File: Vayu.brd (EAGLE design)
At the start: 27 x 80 mm, 63 parts, among them J1 1770911, J2 1770911, J3 3220-10-0100-00, J4 SM04B-SRSS-TB(LF)(SN), Q1 IRLML6402TRPBF, Q2 IRLML6402TRPBF, Q3 IRLML6402TRPBF, Q4 IRLML6402TRPBF, SW1 TL1105LF160Q, SW2 TL1105LF160Q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

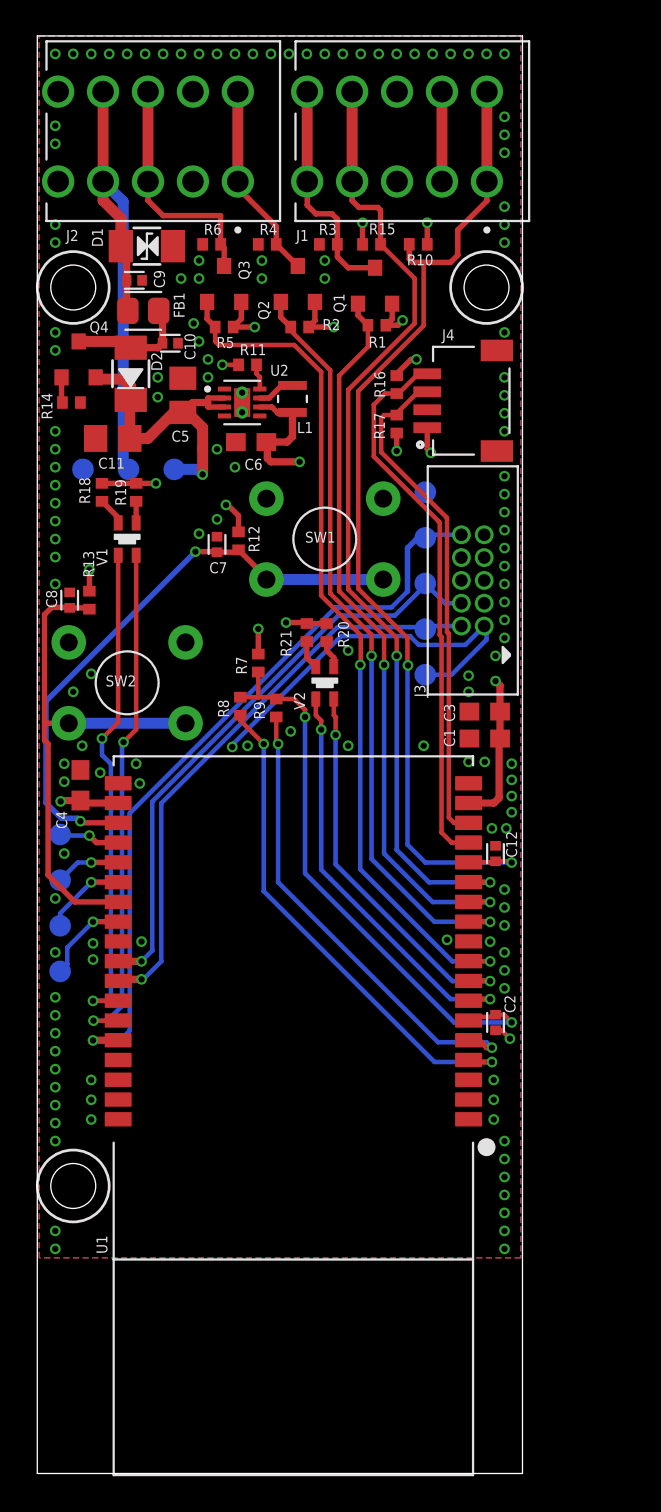
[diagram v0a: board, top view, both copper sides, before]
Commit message: removed sch bugs and WIP in brd
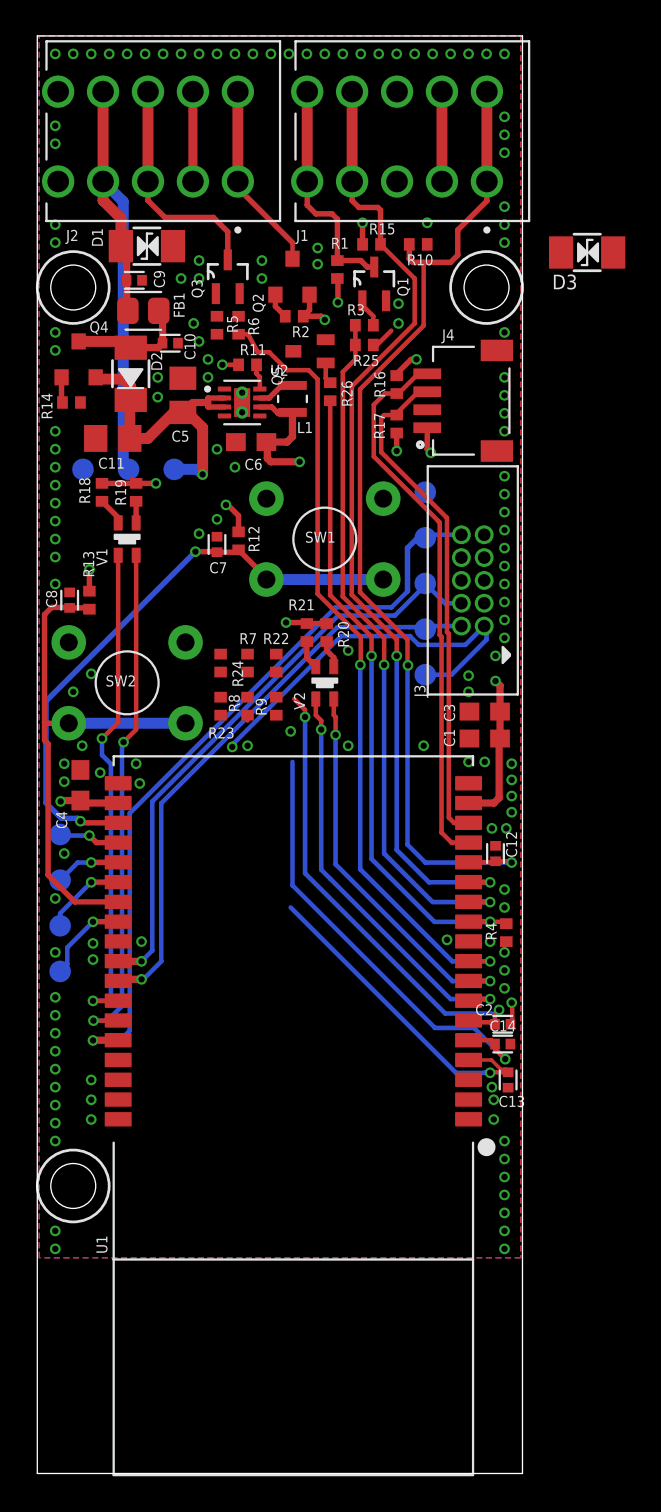
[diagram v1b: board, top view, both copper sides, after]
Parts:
- added C13, C14: 1nF, rcl:CAPC1005X55N
- added D3: SMF12CA, diodes:SOD-123F-BI
- added Q5: MMBT4401WT1G, transistors-BJT:SOT323-BEC
- added R22: 470E, rcl:R0402
- added R23, R25: 100K, rcl:R0402
- added R24: 470K, rcl:R0402
- added R26: 1K, rcl:R0402
- Q1, Q3: value IRLML6402TRPBF -> BSS138PW; device mosfets:SOT23-3 -> mosfets:SC-70_SOT323
- R1: value 1M -> 100K
- R10: value 100K -> 470E
- R3: value 300K -> 1K
- R4, R6: value 300K -> 100K
- R5: value 1M -> 1K
- R7: value 200K -> 47K
- moved R4 40.5 mm to (26.1, 30.1), turned to 90 degrees
- moved R3 4.92 mm to (18.2, 63.9), turned to 180 degrees
- moved R6 4.74 mm to (11.2, 63.9), turned to 270 degrees
- moved R1 3.80 mm to (16.7, 67.0), turned to 270 degrees
- moved R2 0.67 mm to (14.3, 64.4)
- moved R7 0.60 mm to (11.7, 45.1)
- moved Q2 0.50 mm to (14.2, 66.6)
- moved Q3 0.45 mm to (10.6, 66.6), turned to 90 degrees
- moved R5 0.41 mm to (10.0, 63.9), turned to 90 degrees
- moved C2 0.41 mm to (25.9, 25.0), turned to 0 degrees
- moved R8 0.40 mm to (11.7, 42.7)
- moved Q1 0.11 mm to (18.8, 66.2), turned to 90 degrees
- moved R9 0.10 mm to (13.3, 42.7)
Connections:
- removed net !BOARD_NTC_ENABLE: R9.1, U1.5
- removed net !HEATER_ENABLE: Q3.G, R5.1, U1.9
- removed net !SUPPLY_SENSE_ENABLE: R8.1, U1.4
- removed net BOARD_SUPPLY_TEMP_ADC: C2.1, R7.1, R8.2, R9.2, U1.6
- new net BOARD_12V_ADC: C13.1, R23.2, R24.1, U1.4
- new net BOARD_NTC_ADC: C14.1, R22.1, R9.2, U1.5
- new net BOARD_SUPPLY_ADC: C2.1, R7.1, R8.2, U1.6
- new net HEATER_PWM: R5.1, R6.2, U1.9
- new net N$1: Q1.1, R3.1
- new net N$2: Q3.1, R5.2
- new net N$5: Q5.B, R26.1
- new net PMOSFET_EN: Q2.G, Q5.C, R2.1
- net !FAN_ENABLE: now also R26.2, R4.2; no longer Q2.G, R2.1
- net !FAN_PWM: now also R25.1, R3.2; no longer Q1.G, R1.1
- net FAN_SPEED: now also Q1.3, R1.1; no longer Q1.D, R3.2
- net FAN_SUPPLY: now also D3.1; no longer R4.2
- net GND: now also C13.2, C14.2, D3.2, Q1.2, Q3.2, Q5.E, R23.1, R25.2, R8.1, R9.1; no longer J2.2_1, J2.2_2, R3.1
- net HEATER: now also Q3.3; no longer Q3.D, R6.2
- net VDD: now also J2.2_1, J2.2_2, R24.2; no longer Q1.S, Q3.S, R5.2
- net VDDMAIN: now also R22.2
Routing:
- net !HEATER_ENABLE: track 48.1 -> 0.00 mm, vias 2 -> 0
- net HEATER_PWM: track 0.00 -> 44.4 mm, vias 0 -> 2
- net BOARD_SUPPLY_TEMP_ADC: track 32.0 -> 0.00 mm, vias 2 -> 0
- net !SUPPLY_SENSE_ENABLE: track 28.3 -> 0.00 mm, vias 2 -> 0
- net !BOARD_NTC_ENABLE: track 26.4 -> 0.00 mm, vias 2 -> 0
- net BOARD_SUPPLY_ADC: track 0.00 -> 26.4 mm, vias 0 -> 2
- net BOARD_NTC_ADC: track 0.00 -> 25.4 mm, vias 0 -> 1
- net BOARD_12V_ADC: track 0.00 -> 18.4 mm, vias 0 -> 1
- net !FAN_ENABLE: track 42.3 -> 36.6 mm
- net VDD: track 51.5 -> 55.1 mm, vias 4 -> 3
- net VCC_+3.3V: track 42.1 -> 39.1 mm, vias 13 -> 12
- net GND: track 5.99 -> 7.89 mm, vias 142 -> 143
- net !FAN_PWM: track 40.7 -> 38.9 mm
- net N$1: track 0.00 -> 1.61 mm
- net PMOSFET_EN: track 0.00 -> 1.43 mm
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
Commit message: bug fix, updated MOSFET driver and other MOSFETS, added SWO support
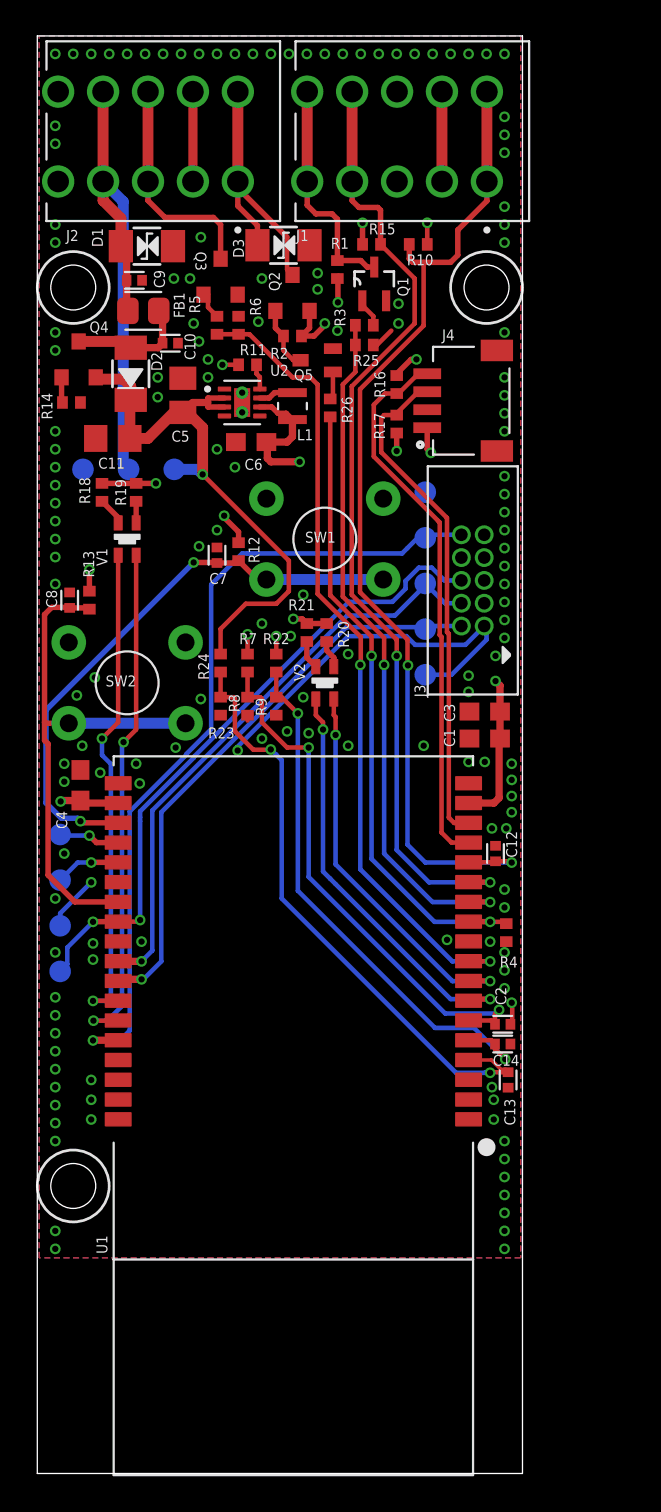
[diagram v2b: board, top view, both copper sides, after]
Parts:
- Q3: value BSS138PW -> DMN2056U; device mosfets:SC-70_SOT323 -> mosfets:SOT23-3
- R10, R22: value 470E -> 200K
- R23: value 100K -> 10K
- R24: value 470K -> 47K
- R26, R3, R5: value 1K -> 10K
- moved D3 16.9 mm to (13.7, 68.3)
- moved R2 1.10 mm to (14.2, 63.3)
- moved R26 0.90 mm to (16.3, 59.3)
- moved Q2 0.90 mm to (14.2, 65.7)
- moved Q5 0.64 mm to (15.6, 62.0)
- moved C7 0.60 mm to (10.0, 51.1)
- moved R12 0.60 mm to (11.2, 51.3)
- moved Q3 0.40 mm to (10.2, 66.6), turned to 0 degrees
- moved L1 0.40 mm to (14.2, 59.4)
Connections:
- removed net SERIAL_CTS: TP8.1, U1.26
- removed net SERIAL_RTS: TP9.1, U1.24
- new net JTAG_SWO: J3.6, TP8.1, U1.26
- net GND: now also Q3.S, TP9.1; no longer Q3.2
- net HEATER: now also Q3.D; no longer Q3.3
- net N$2: now also Q3.G; no longer Q3.1
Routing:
- net JTAG_SWO: track 0.00 -> 36.3 mm, vias 0 -> 2
- net BOARD_12V_ADC: track 18.4 -> 34.1 mm, vias 1 -> 2
- net VDD: track 55.1 -> 70.7 mm
- net VDDMAIN: track 36.4 -> 44.8 mm, vias 2 -> 3
- net BOARD_NTC_ADC: track 25.4 -> 30.9 mm, vias 1 -> 2
- net SERIAL_CTS: track 4.92 -> 0.00 mm, vias 1 -> 0
- net SERIAL_RTS: track 4.64 -> 0.00 mm, vias 1 -> 0
- net FAN_SUPPLY: track 10.6 -> 15.1 mm
- net BOARD_SUPPLY_ADC: track 26.4 -> 30.2 mm
- net !RESET: track 42.1 -> 45.5 mm
- net GND: track 7.89 -> 11.0 mm, vias 143 -> 152
- net VCC_+3.3V: track 39.1 -> 42.1 mm, vias 12 -> 13
- net PMOSFET_EN: track 1.43 -> 3.56 mm
- net N$2: track 0.00 -> 1.68 mm
- net !FAN_ENABLE: track 36.6 -> 35.7 mm
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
